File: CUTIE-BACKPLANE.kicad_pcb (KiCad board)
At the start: 4 copper layers, 50.5 x 59.9 mm, 22 parts, among them J1 USB3_A, J2 ERF8-025-05.0-L-DV-L-K-TR, J3 ERF8-025-05.0-L-DV-L-K-TR, J4 ERF8-025-05.0-L-DV-L-K-TR

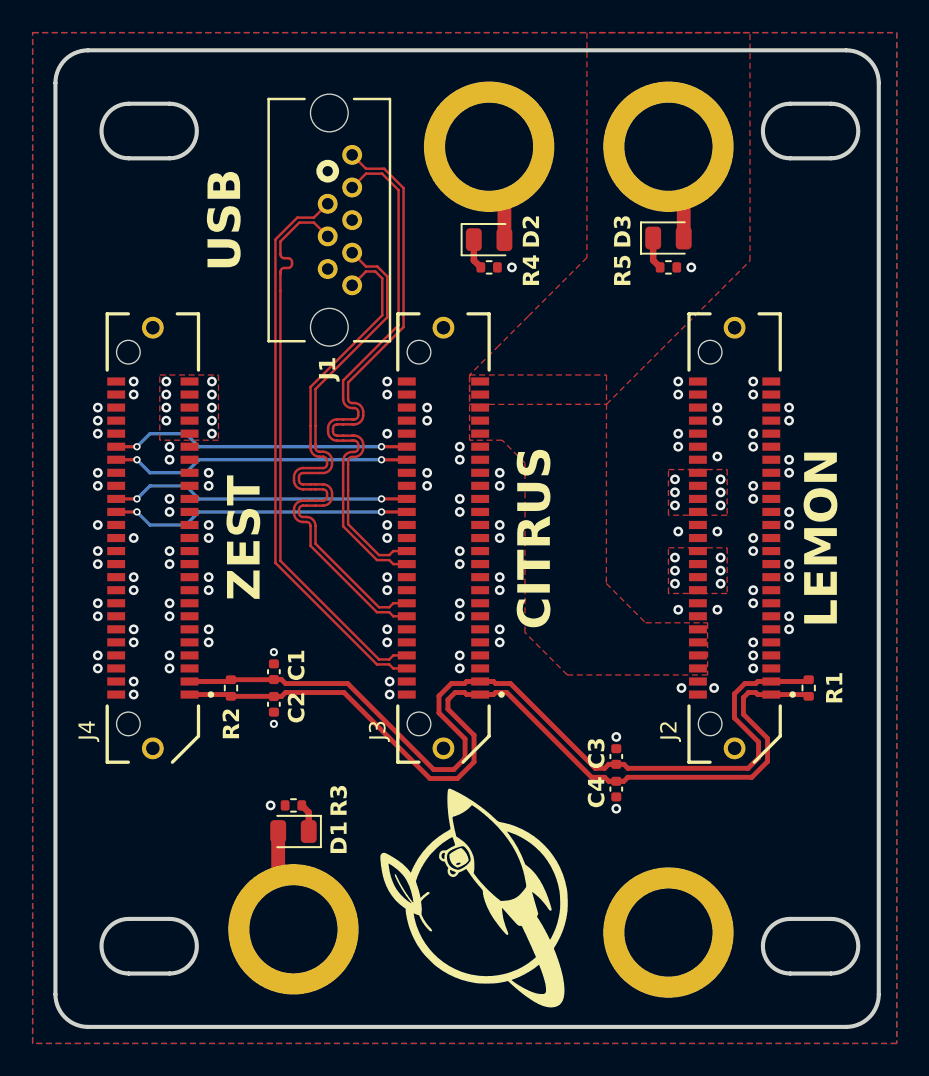
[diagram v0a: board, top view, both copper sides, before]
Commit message: fillet traces
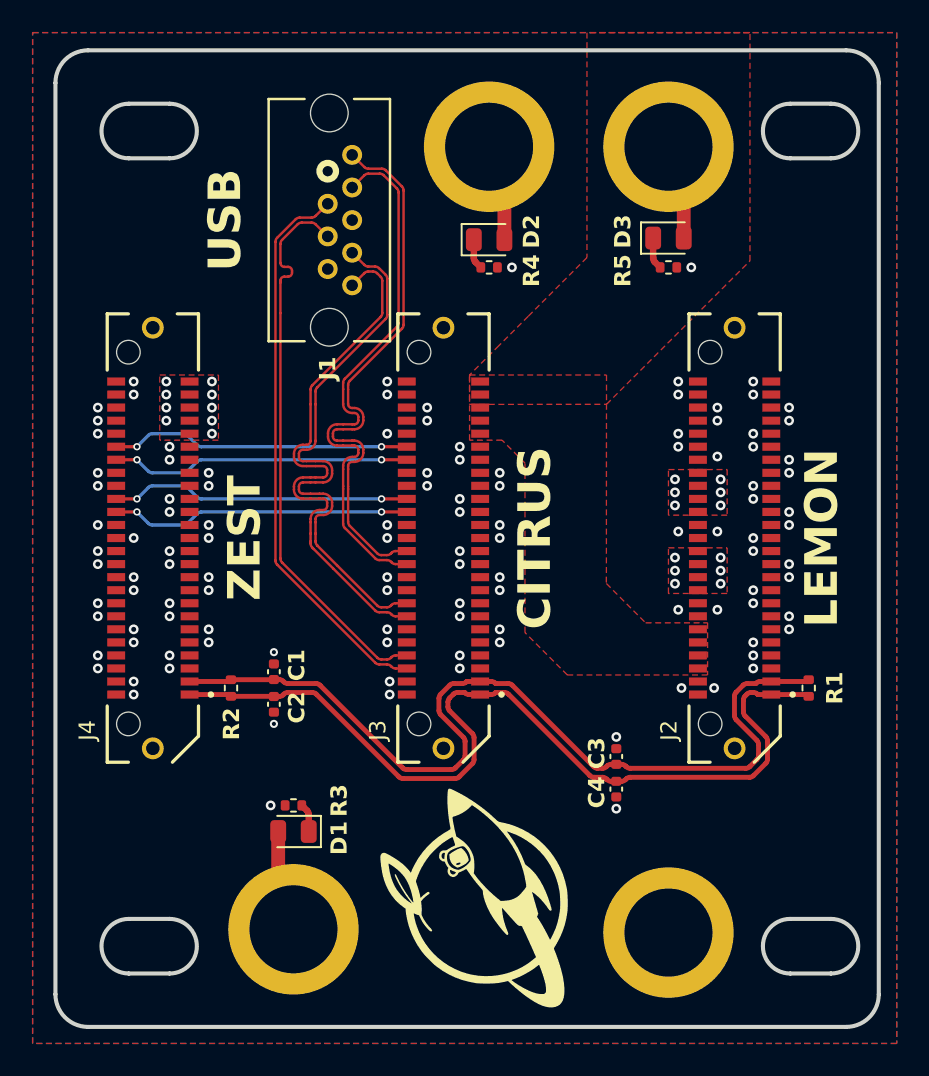
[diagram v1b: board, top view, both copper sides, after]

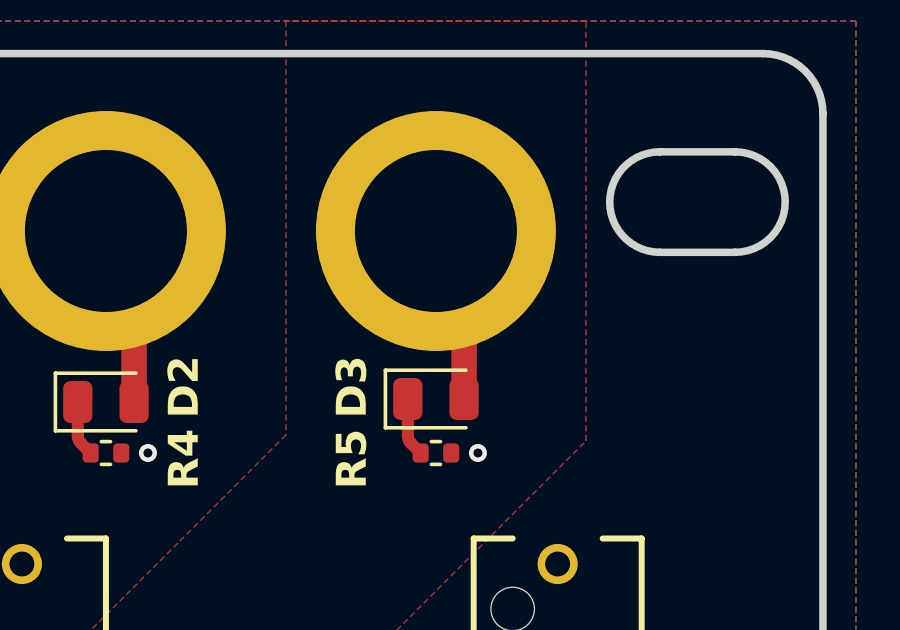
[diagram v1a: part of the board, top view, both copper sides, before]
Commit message: edited silkscreens for fab
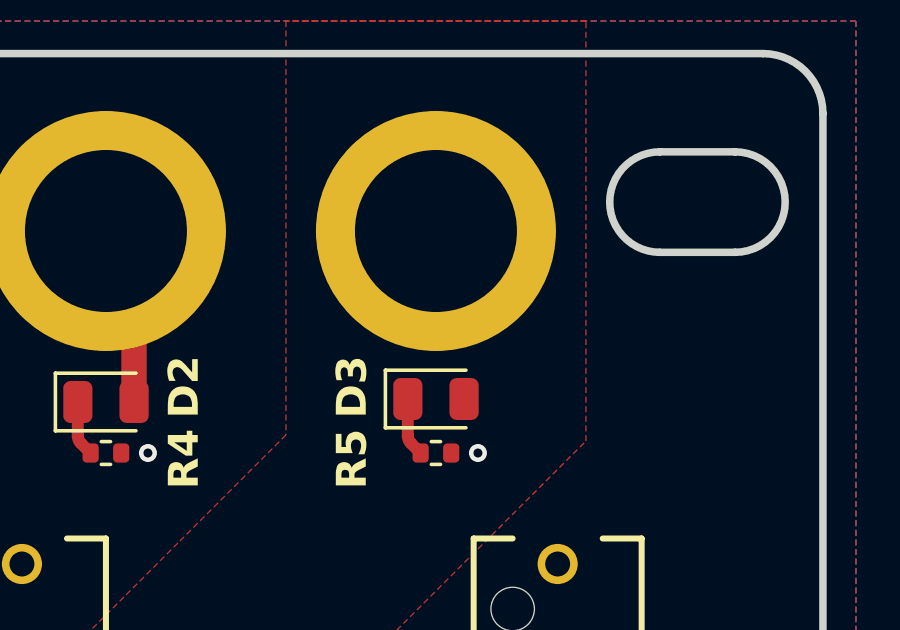
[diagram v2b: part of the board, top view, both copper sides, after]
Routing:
- net /CITRUS/5V0: track 5.97 -> 0.00 mm
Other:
- board text removed: "hsp payload apr 2026"
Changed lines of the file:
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@@
 		)
 	)
-	(gr_text "hsp payload apr 2026"
-		(at 121.6 74.007999 90)
-		(layer "B.SilkS")
-		(effects
-			(font
-				(size 0.8 0.8)
-				(thickness 0.15)
-				(bold yes)
-			)
-			(justify left bottom mirror)
-		)
-	)
 	(gr_text "Board"
 		(at 74.2 89.9375 90)
@@
 		(net "/CITRUS/CMRF.CS0n")
 	)
-	(segment
-		(start 110.834987 72.834987)
-		(end 110 72)
-		(width 0.85)
-		(layer "F.Cu")
-		(net "/CITRUS/5V0")
-	)
-	(segment
-		(start 110.9375 77.6)
-		(end 110.9375 73.082475)
-		(width 0.85)
-		(layer "F.Cu")
-		(net "/CITRUS/5V0")
-	)
-	(arc
-		(start 110.9375 73.082475)
-		(mid 110.910858 72.948535)
-		(end 110.834987 72.834987)
-		(width 0.85)
-		(layer "F.Cu")
-		(net "/CITRUS/5V0")
-	)
 	(zone
